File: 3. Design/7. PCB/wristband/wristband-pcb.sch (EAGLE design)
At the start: 44 parts, among them IC2 MAX16150AUT+T, IC5 STM32F051K6U6, Q1 2N7002NXAKR, Y2 FA-20H_16.0000MF12Z-AC3, Y3 FA-20H_16.0000MF12Z-AC3

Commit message: UPDT: Added all work done on the Wristband PCB board so far
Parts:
- removed IC5: STM32F051K6U6, STM32F051K6U6:STM32F051K6U6
- added IC1: STM32F051K8T6, stm32f051k8t6:STM32F051K8T6
- renumbered IC2 to PB_CTRL, U$4 to C17, U$5 to C18, U$6 to C16, U$7 to C15
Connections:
- net GND: now also IC1.VSS_1, IC1.VSS_2; no longer IC5.VSS/VSSA_(EP)
- net LED_CONN_PROB: now also IC1.PA15; no longer IC5.PB3
- net LED_PWR: now also IC1.PB3; no longer IC5.PB4
- net MPU_6050_INT: now also IC1.PB4; no longer IC5.PB5
- net MPU_6050_SCL: now also IC1.PB5; no longer IC5.PB6
- net MPU_6050_SDA: now also IC1.PB6; no longer IC5.PB7
- net N$4: now also IC1.PB7; no longer IC5.BOOT0
- net NRF24L01_CE: now also IC1.PB1; no longer IC5.PB1
- net NRF24L01_CRYSTAL1: now also C16.1, Y3.CRYSTAL_2; no longer C15.1, Y3.CRYSTAL_1
- net NRF24L01_CRYSTAL2: now also C15.1, Y3.CRYSTAL_1; no longer C16.1, Y3.CRYSTAL_2
- net NRF24L01_CSN: now also IC1.PB0; no longer IC5.PB0
- net NRF24L01_IRQ: now also IC1.PA4; no longer IC5.PB2
- net NRF24L01_MISO: now also IC1.PA6; no longer IC5.PA6
- net NRF24L01_MOSI: now also IC1.PA7; no longer IC5.PA7
- net NRF24L01_SCK: now also IC1.PA5; no longer IC5.PA5
- net PWR_CLR: now also IC1.PA0; no longer IC5.PA0
- net PWR_INT: now also IC1.PA1; no longer IC5.PA1
- net STM32F051_CRYSTAL1: now also IC1.PF0/OSC_IN; no longer IC5.PF0/OSC_IN
- net STM32F051_CRYSTAL2: now also IC1.PF1/OSC_OUT; no longer IC5.PF1/OSC_OUT
- net SYS_NRST: now also IC1.NRST; no longer IC5.NRST
- net SYS_SWCLK: now also IC1.PA14; no longer IC5.PA14
- net SYS_SWDIO: now also IC1.PA13; no longer IC5.PA13
- net VDD: now also IC1.VDD_1, IC1.VDD_2; no longer IC5.VDD_1, IC5.VDD_2
- net VDDA: now also IC1.VDDA; no longer IC5.VDDA
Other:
- moved on the sheet: R7

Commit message: UPDT: PCB Wristband
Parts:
- removed U$10, U$13: 1uF [0603], Nordic_nRF:CAPACITOR_0603_L
- removed U$12, U$15: 4.7nF [0805], Nordic_nRF:CAPACITOR_0805_L
- added PS1: AP22814AW5-7, AP22814AW5-7:AP22814AW5-7
- added U$3, U$4: 4.7uF [0603], Nordic_nRF:CAPACITOR_0603_L
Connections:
- net GND: now also U$3.2, U$4.2; no longer U$10.2, U$12.2, U$13.2, U$15.2
- net VDD: now also U$3.1, U$4.1; no longer U$10.1, U$12.1, U$13.1, U$15.1
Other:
- moved on the sheet: C3, U$11, U$14

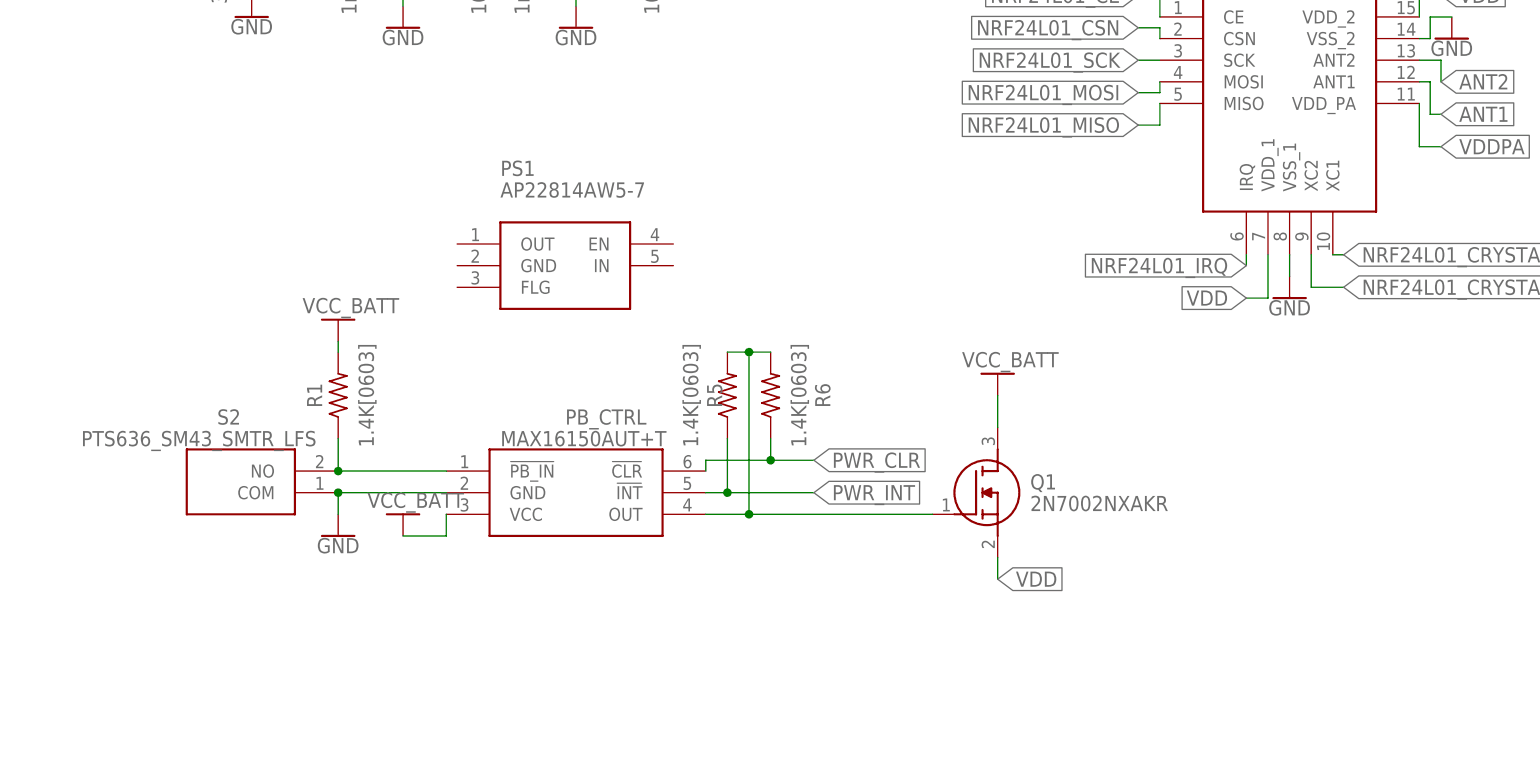
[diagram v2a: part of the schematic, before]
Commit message: UPDT: Added Load Switch to Wristband PCB
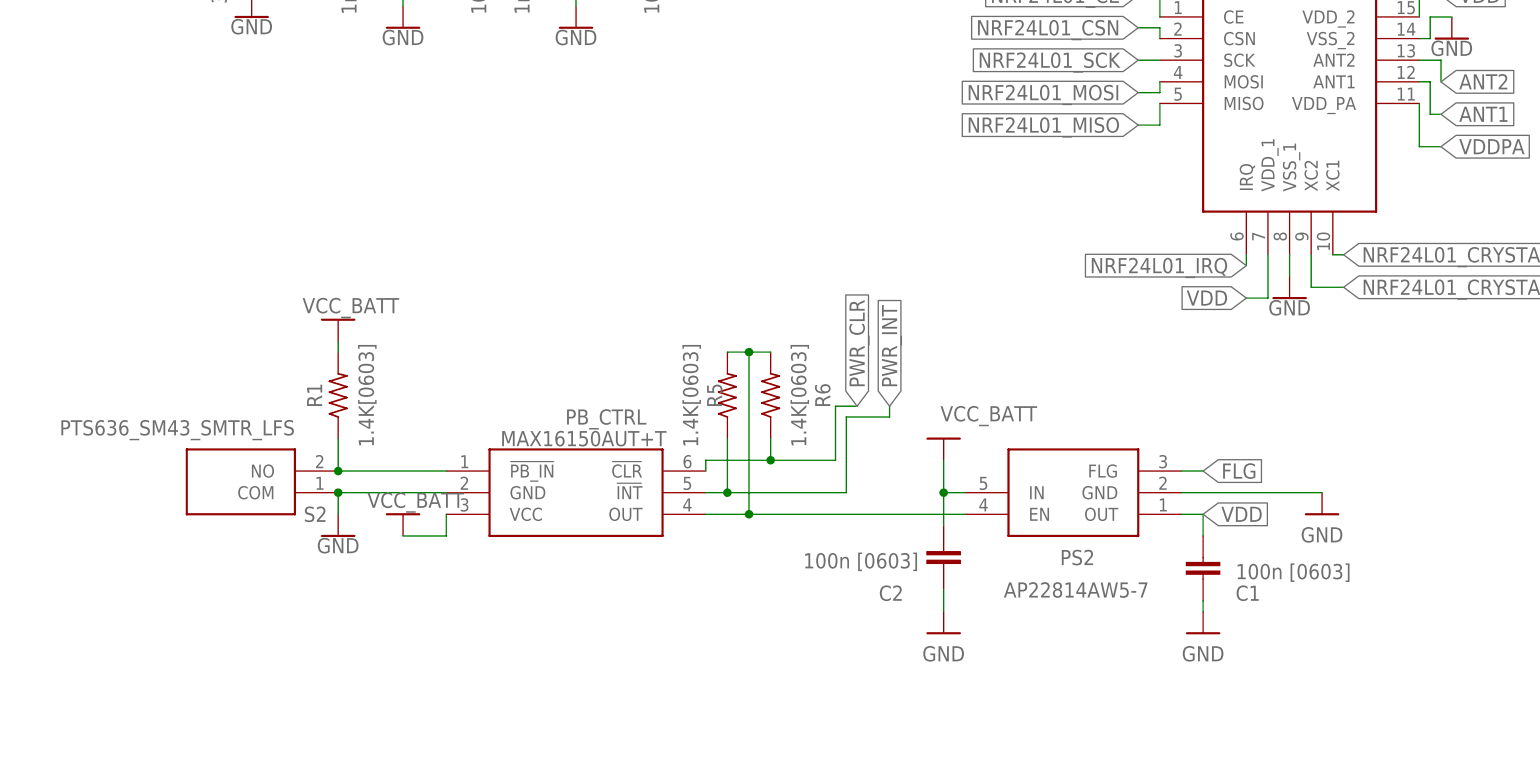
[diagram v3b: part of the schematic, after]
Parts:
- removed PS1: AP22814AW5-7, AP22814AW5-7:AP22814AW5-7
- removed Q1: 2N7002NXAKR, 2N7002NXAKR:2N7002NXAKR
- added C1, C2: 100n [0603], Capacitor:C_CHIP-0603(1608-METRIC)
- added PS2: AP22814AW5-7, AP22814AW5-7:AP22814AW5-7
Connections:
- new net FLG: PS2.FLG
- net GND: now also C1.2, C2.2, PS2.GND
- net N$5: now also PS2.EN; no longer Q1.G
- net VCC_BATT: now also C2.1, PS2.IN; no longer Q1.D
- net VDD: now also C1.1, PS2.OUT; no longer Q1.S

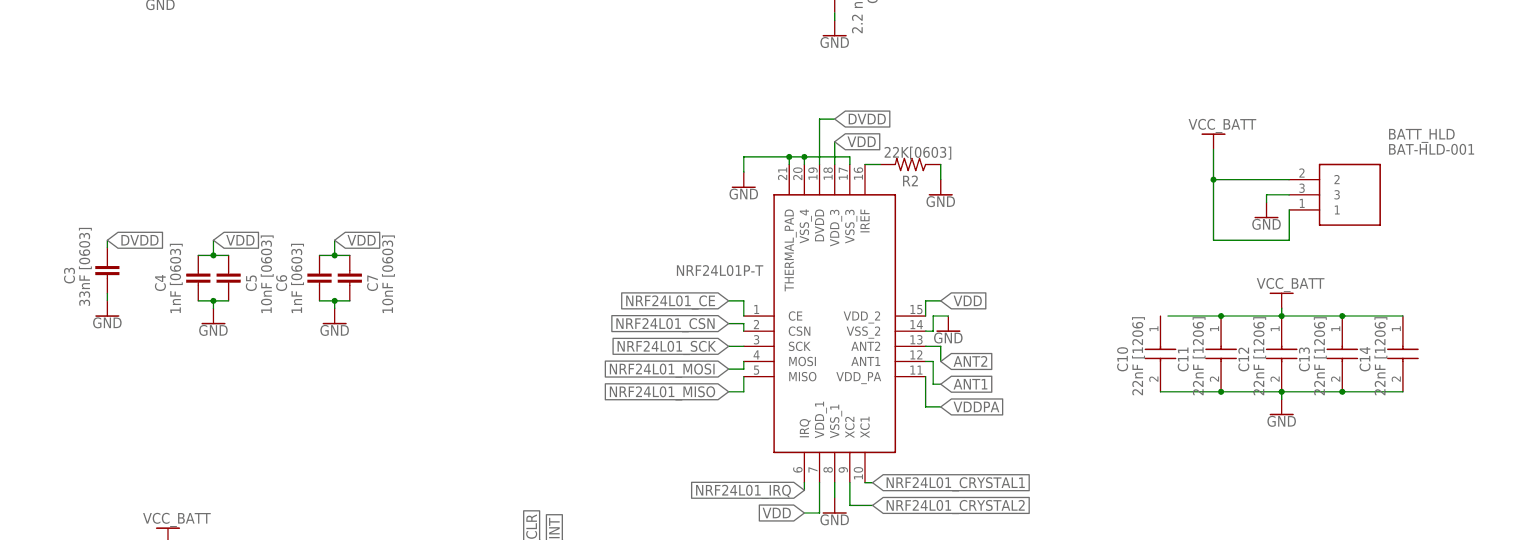
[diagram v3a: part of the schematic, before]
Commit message: UPDT: Updated wristband PCB design with new connections and slightly different layout
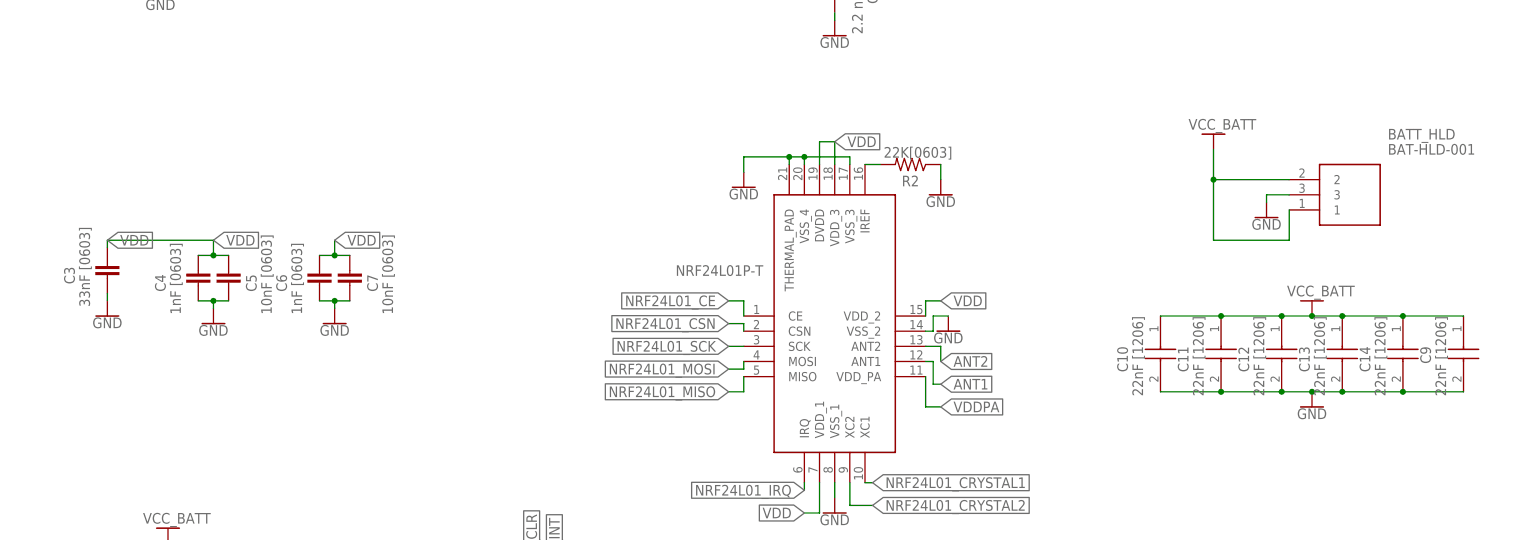
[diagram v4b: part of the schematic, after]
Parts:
- added C9: 22nF [1206], CL31B226KPHNNNE:CL31B226KPHNNNE
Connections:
- removed net DVDD: C3.1, NRF24L01+.DVDD
- net GND: now also C9.2
- net VCC_BATT: now also C10.1, C9.1
- net VDD: now also C3.1, NRF24L01+.DVDD

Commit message: UPDT: Wristband PCB
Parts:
- removed C9: 22nF [1206], CL31B226KPHNNNE:CL31B226KPHNNNE
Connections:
- net N$5 renamed PWR_EN
- net GND: no longer C9.2
- net VCC_BATT: no longer C9.1
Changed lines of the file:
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@@
 <part name="GND29" library="SparkFun-PowerSymbols" library_urn="urn:adsk.eagle:library:530" deviceset="GND" device=""/>
 <part name="VCC_BATT6" library="mpad_v2.1" deviceset="VCC_BATT" device=""/>
-<part name="C9" library="CL31B226KPHNNNE" deviceset="CL31B226KPHNNNE" device="" override_package3d_urn="urn:adsk.eagle:package:25483761/2" override_package_urn="urn:adsk.eagle:footprint:25483762/1" value="22nF [1206]"/>
 </parts>
 <sheets>
@@
 <attribute name="VALUE" x="-13.081" y="65.532" size="1.778" layer="96"/>
 </instance>
-<instance part="C9" gate="G$1" x="133.35" y="113.03" smashed="yes" rot="R270">
-<attribute name="NAME" x="127" y="107.95" size="1.778" layer="95" rot="R270" align="center-left"/>
-<attribute name="VALUE" x="129.54" y="113.03" size="1.778" layer="96" rot="R270" align="center-left"/>
-</instance>
 </instances>
 <busses>
@@
 <wire x1="113.03" y1="100.33" x2="123.19" y2="100.33" width="0.1524" layer="91"/>
 <junction x="113.03" y="100.33"/>
-<pinref part="C9" gate="G$1" pin="2"/>
-<wire x1="123.19" y1="100.33" x2="133.35" y2="100.33" width="0.1524" layer="91"/>
-<junction x="123.19" y="100.33"/>
 <pinref part="GND22" gate="1" pin="GND"/>
 <junction x="107.95" y="100.33"/>
@@
 <wire x1="113.03" y1="113.03" x2="123.19" y2="113.03" width="0.1524" layer="91"/>
 <junction x="113.03" y="113.03"/>
-<pinref part="C9" gate="G$1" pin="1"/>
-<wire x1="123.19" y1="113.03" x2="133.35" y2="113.03" width="0.1524" layer="91"/>
-<junction x="123.19" y="113.03"/>
 <pinref part="VCC_BATT5" gate="VCC_BAT" pin="VCC_BATT"/>
 <junction x="107.95" y="113.03"/>
@@
 </segment>
 </net>
-<net name="N$5" class="0">
+<net name="PWR_EN" class="0">
 <segment>
 <pinref part="R5" gate="G$1" pin="2"/>
@@
 <wire x1="-35.56" y1="54.61" x2="-10.16" y2="54.61" width="0.1524" layer="91"/>
 <junction x="-35.56" y="54.61"/>
-</segment>
-</net>
+<label x="-33.02" y="54.61" size="1.778" layer="95" rot="R270" xref="yes"/>
+</segment>
+</net>

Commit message: UPDT: Further updates to the wristband PCB
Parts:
- removed U$2: MIFA-CYPRESS-2, MIFA:MIFA-CYPRESS-2
- added MIFA: MIFA-CYPRESS-2, MIFA:MIFA-CYPRESS-2
- renumbered U$11 to C22, U$14 to C21, U$3 to C19, U$4 to C20, U$8 to C23, U$9 to C24
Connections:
- removed net N$1: ANT1.UNBALANCED_PORT, U$2.ANT
- removed net VDDA: C23.1, C24.1, IC1.VDDA
- new net MIFA: ANT1.UNBALANCED_PORT, MIFA.ANT
- net GND: now also MIFA.GND; no longer U$2.GND
- net VDD: now also C23.1, C24.1, IC1.VDDA
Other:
- moved on the sheet: R7

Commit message: UPDT: Wristband PCB
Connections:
- net GND: now also MPU_6050_IF.5; no longer MPU_6050_IF.4
- net MPU_6050_INT: now also MPU_6050_IF.4; no longer MPU_6050_IF.5
- net MPU_6050_SCL: now also MPU_6050_IF.3; no longer MPU_6050_IF.2
- net MPU_6050_SDA: now also MPU_6050_IF.2; no longer MPU_6050_IF.3
- net SYS_NRST: now also PROG_IF.2; no longer PROG_IF.4
- net SYS_SWCLK: now also PROG_IF.3; no longer PROG_IF.2
- net SYS_SWDIO: now also PROG_IF.4; no longer PROG_IF.3
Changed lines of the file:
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@@
 <attribute name="VALUE" x="81.28" y="317.5" size="1.778" layer="96" rot="R180" align="center-left"/>
 </instance>
-<instance part="GND9" gate="1" x="102.87" y="328.93" smashed="yes">
-<attribute name="VALUE" x="102.87" y="331.216" size="1.778" layer="96" align="top-center"/>
+<instance part="GND9" gate="1" x="109.22" y="330.2" smashed="yes">
+<attribute name="VALUE" x="109.22" y="335.026" size="1.778" layer="96" align="top-center"/>
 </instance>
 <instance part="FRAME2" gate="G$1" x="-119.38" y="213.36" smashed="yes"/>
@@
 <pinref part="GND8" gate="1" pin="GND"/>
 <wire x1="100.33" y1="350.52" x2="100.33" y2="349.25" width="0.1524" layer="91"/>
-</segment>
-<segment>
-<pinref part="MPU_6050_IF" gate="G$1" pin="4"/>
-<wire x1="97.79" y1="330.2" x2="97.79" y2="331.47" width="0.1524" layer="91"/>
-<pinref part="GND9" gate="1" pin="GND"/>
-<wire x1="97.79" y1="331.47" x2="102.87" y2="331.47" width="0.1524" layer="91"/>
 </segment>
 <segment>
@@
 <junction x="107.95" y="100.33"/>
 </segment>
+<segment>
+<pinref part="MPU_6050_IF" gate="G$1" pin="5"/>
+<pinref part="GND9" gate="1" pin="GND"/>
+<wire x1="97.79" y1="332.74" x2="109.22" y2="332.74" width="0.1524" layer="91"/>
+</segment>
 </net>
 <net name="N$2" class="0">
@@
 <segment>
 <pinref part="MPU_6050_IF" gate="G$1" pin="1"/>
-<wire x1="97.79" y1="322.58" x2="100.33" y2="322.58" width="0.1524" layer="91"/>
-<label x="104.14" y="320.04" size="1.778" layer="95" xref="yes"/>
-<wire x1="100.33" y1="322.58" x2="100.33" y2="320.04" width="0.1524" layer="91"/>
-<wire x1="100.33" y1="320.04" x2="104.14" y2="320.04" width="0.1524" layer="91"/>
+<wire x1="97.79" y1="322.58" x2="97.79" y2="314.96" width="0.1524" layer="91"/>
+<label x="107.95" y="314.96" size="1.778" layer="95" xref="yes"/>
+<wire x1="97.79" y1="314.96" x2="107.95" y2="314.96" width="0.1524" layer="91"/>
 </segment>
 <segment>
@@
 <net name="SYS_NRST" class="0">
 <segment>
-<pinref part="PROG_IF" gate="G$1" pin="4"/>
-<label x="100.33" y="359.41" size="1.778" layer="95" xref="yes"/>
-<wire x1="97.79" y1="358.14" x2="100.33" y2="358.14" width="0.1524" layer="91"/>
-<wire x1="100.33" y1="358.14" x2="100.33" y2="359.41" width="0.1524" layer="91"/>
-</segment>
-<segment>
 <wire x1="-15.24" y1="309.88" x2="-27.94" y2="309.88" width="0.1524" layer="91"/>
 <wire x1="-27.94" y1="309.88" x2="-27.94" y2="308.61" width="0.1524" layer="91"/>
@@
 <pinref part="IC1" gate="G$1" pin="NRST"/>
 </segment>
+<segment>
+<label x="110.49" y="350.52" size="1.778" layer="95" xref="yes"/>
+<pinref part="PROG_IF" gate="G$1" pin="2"/>
+<wire x1="109.22" y1="350.52" x2="110.49" y2="350.52" width="0.1524" layer="91"/>
+<wire x1="97.79" y1="353.06" x2="109.22" y2="353.06" width="0.1524" layer="91"/>
+<wire x1="109.22" y1="353.06" x2="109.22" y2="350.52" width="0.1524" layer="91"/>
+</segment>
 </net>
 <net name="SYS_SWDIO" class="0">
-<segment>
-<pinref part="PROG_IF" gate="G$1" pin="3"/>
-<wire x1="97.79" y1="355.6" x2="100.33" y2="355.6" width="0.1524" layer="91"/>
-<label x="100.33" y="355.6" size="1.778" layer="95" xref="yes"/>
-</segment>
 <segment>
 <wire x1="22.86" y1="314.96" x2="25.4" y2="314.96" width="0.1524" layer="91"/>
@@
 <pinref part="IC1" gate="G$1" pin="PA13"/>
 </segment>
+<segment>
+<label x="110.49" y="358.14" size="1.778" layer="95" xref="yes"/>
+<pinref part="PROG_IF" gate="G$1" pin="4"/>
+<wire x1="97.79" y1="358.14" x2="110.49" y2="358.14" width="0.1524" layer="91"/>
+</segment>
 </net>
 <net name="SYS_SWCLK" class="0">
-<segment>
-<pinref part="PROG_IF" gate="G$1" pin="2"/>
-<label x="100.33" y="351.79" size="1.778" layer="95" xref="yes"/>
-<wire x1="97.79" y1="353.06" x2="100.33" y2="353.06" width="0.1524" layer="91"/>
-<wire x1="100.33" y1="353.06" x2="100.33" y2="351.79" width="0.1524" layer="91"/>
-</segment>
 <segment>
 <wire x1="22.86" y1="317.5" x2="25.4" y2="317.5" width="0.1524" layer="91"/>
@@
 <pinref part="IC1" gate="G$1" pin="PA14"/>
 </segment>
+<segment>
+<label x="110.49" y="354.33" size="1.778" layer="95" xref="yes"/>
+<wire x1="109.22" y1="355.6" x2="110.49" y2="355.6" width="0.1524" layer="91"/>
+<wire x1="110.49" y1="355.6" x2="110.49" y2="354.33" width="0.1524" layer="91"/>
+<pinref part="PROG_IF" gate="G$1" pin="3"/>
+<wire x1="107.95" y1="355.6" x2="109.22" y2="355.6" width="0.1524" layer="91"/>
+<wire x1="107.95" y1="355.6" x2="97.79" y2="355.6" width="0.1524" layer="91"/>
+</segment>
 </net>
 <net name="MPU_6050_SCL" class="0">
-<segment>
-<pinref part="MPU_6050_IF" gate="G$1" pin="2"/>
-<wire x1="97.79" y1="325.12" x2="100.33" y2="325.12" width="0.1524" layer="91"/>
-<wire x1="100.33" y1="325.12" x2="100.33" y2="323.85" width="0.1524" layer="91"/>
-<label x="104.14" y="323.85" size="1.778" layer="95" xref="yes"/>
-<wire x1="100.33" y1="323.85" x2="104.14" y2="323.85" width="0.1524" layer="91"/>
-</segment>
 <segment>
 <wire x1="5.08" y1="335.28" x2="5.08" y2="349.25" width="0.1524" layer="91"/>
@@
 <pinref part="IC1" gate="G$1" pin="PB5"/>
 </segment>
+<segment>
+<pinref part="MPU_6050_IF" gate="G$1" pin="3"/>
+<wire x1="97.79" y1="327.66" x2="104.14" y2="327.66" width="0.1524" layer="91"/>
+<wire x1="104.14" y1="327.66" x2="104.14" y2="323.85" width="0.1524" layer="91"/>
+<wire x1="104.14" y1="323.85" x2="107.95" y2="323.85" width="0.1524" layer="91"/>
+<label x="107.95" y="323.85" size="1.778" layer="95" xref="yes"/>
+</segment>
 </net>
 <net name="MPU_6050_SDA" class="0">
-<segment>
-<pinref part="MPU_6050_IF" gate="G$1" pin="3"/>
-<label x="104.14" y="327.66" size="1.778" layer="95" xref="yes"/>
-<wire x1="97.79" y1="327.66" x2="104.14" y2="327.66" width="0.1524" layer="91"/>
-</segment>
 <segment>
 <wire x1="2.54" y1="335.28" x2="2.54" y2="353.06" width="0.1524" layer="91"/>
@@
 <pinref part="IC1" gate="G$1" pin="PB6"/>
 </segment>
+<segment>
+<pinref part="MPU_6050_IF" gate="G$1" pin="2"/>
+<wire x1="97.79" y1="325.12" x2="100.33" y2="325.12" width="0.1524" layer="91"/>
+<wire x1="100.33" y1="325.12" x2="100.33" y2="320.04" width="0.1524" layer="91"/>
+<wire x1="100.33" y1="320.04" x2="107.95" y2="320.04" width="0.1524" layer="91"/>
+<label x="107.95" y="320.04" size="1.778" layer="95" xref="yes"/>
+</segment>
 </net>
 <net name="MPU_6050_INT" class="0">
-<segment>
-<pinref part="MPU_6050_IF" gate="G$1" pin="5"/>
-<wire x1="97.79" y1="332.74" x2="104.14" y2="332.74" width="0.1524" layer="91"/>
-<label x="104.14" y="332.74" size="1.778" layer="95" xref="yes"/>
-</segment>
 <segment>
 <label x="13.97" y="345.44" size="1.778" layer="95" xref="yes"/>
@@
 <pinref part="IC1" gate="G$1" pin="PB4"/>
 </segment>
-</net>
+<segment>
+<pinref part="MPU_6050_IF" gate="G$1" pin="4"/>
+<wire x1="97.79" y1="330.2" x2="105.41" y2="330.2" width="0.1524" layer="91"/>
+<wire x1="105.41" y1="330.2" x2="105.41" y2="327.66" width="0.1524" layer="91"/>
+<wire x1="105.41" y1="327.66" x2="107.95" y2="327.66" width="0.1524" layer="91"/>
+<label x="107.95" y="327.66" size="1.778" layer="95" xref="yes"/>
+</segment>
+</net>
